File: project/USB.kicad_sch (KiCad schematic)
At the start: 13 parts, among them IC10 FT232RL, SW6 FT232 RESET, X6 SERIAL

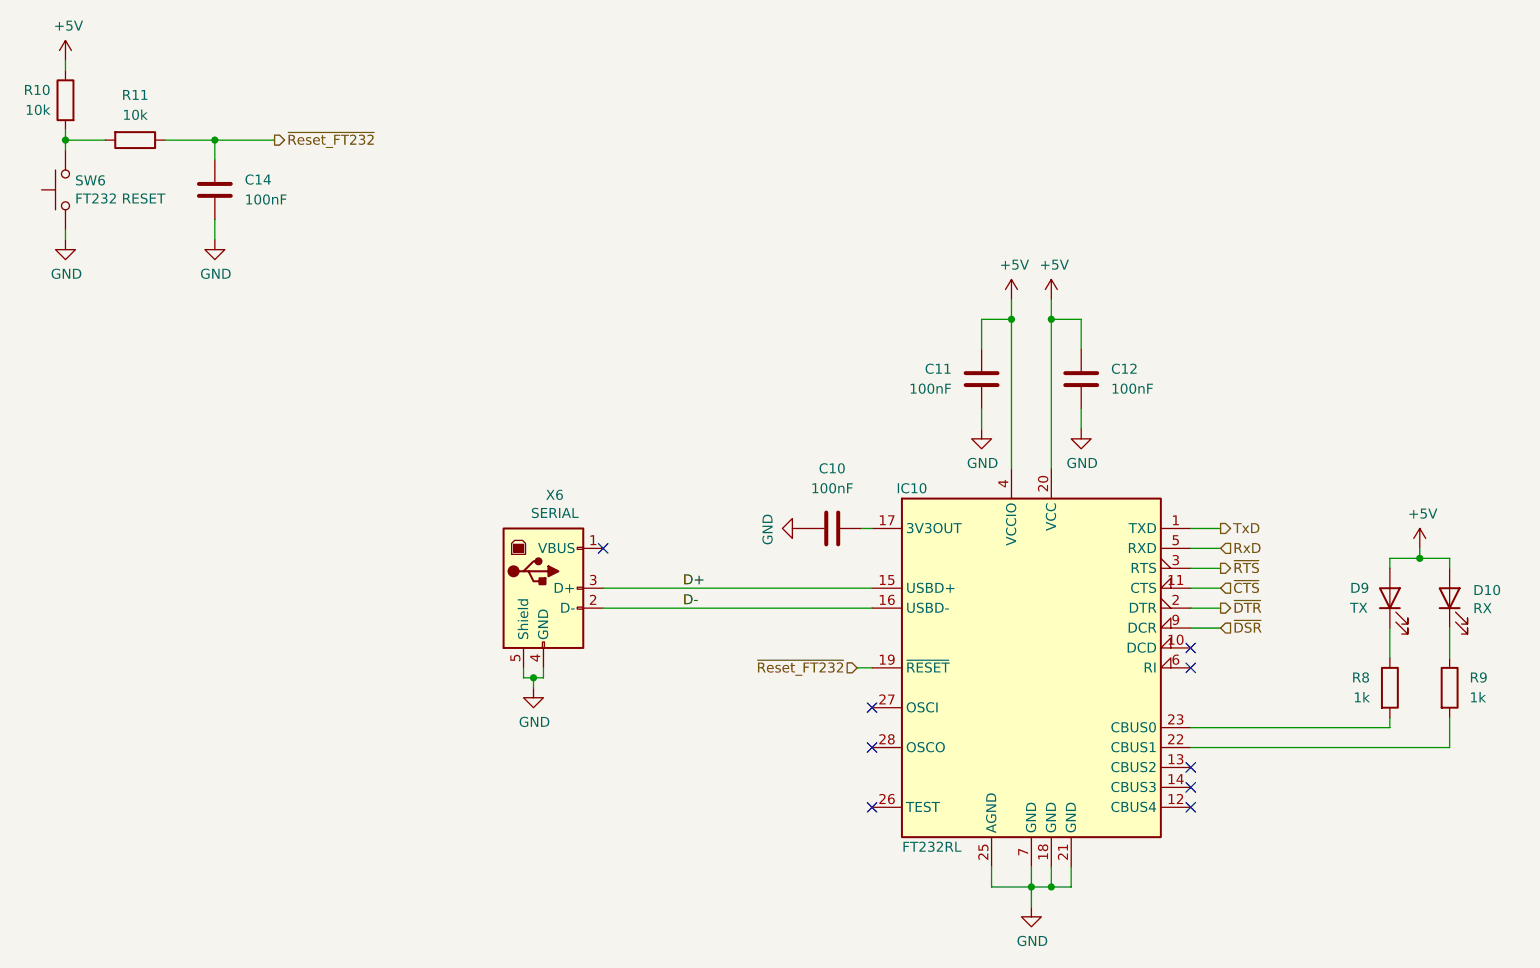
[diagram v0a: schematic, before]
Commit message: Fix grid issues, fix missing libraries, replace FT232 with FT231
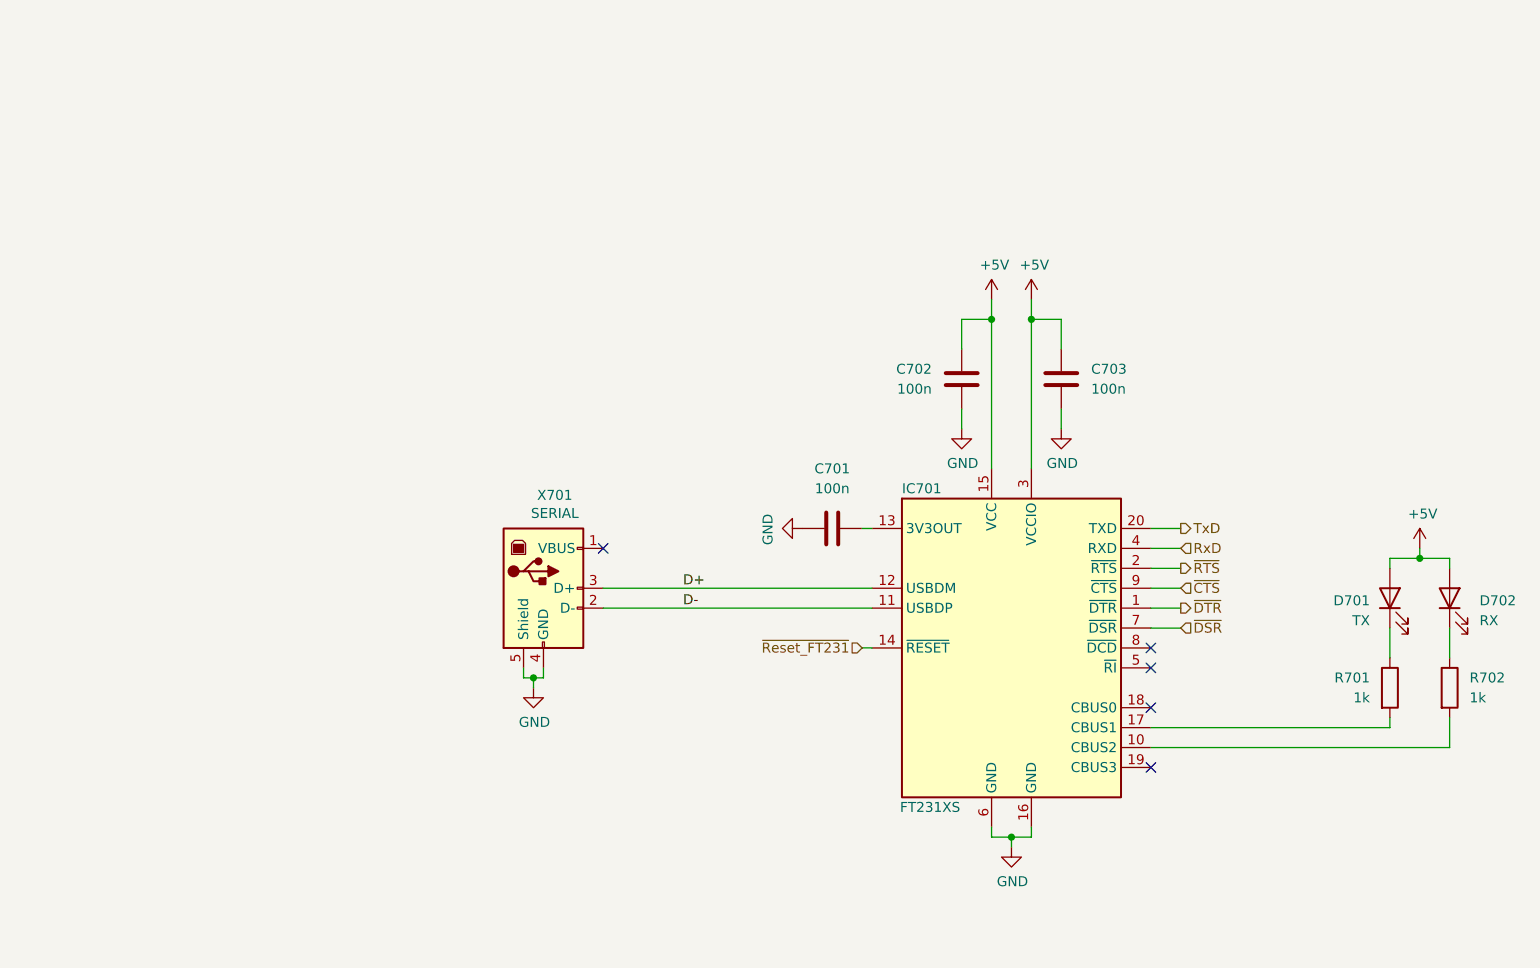
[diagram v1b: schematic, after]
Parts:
- removed C14: 100nF, Capacitor_THT:C_Rect_L4.0mm_W2.5mm_P2.50mm, symbol Device:C
- removed IC10: FT232RL, Package_SO:SSOP-28_5.3x10.2mm_P0.65mm, symbol Interface_USB:FT232RL
- removed R10, R11: 10k, Resistor_THT:R_Axial_DIN0207_L6.3mm_D2.5mm_P7.62mm_Horizontal, symbol Device:R
- removed SW6: FT232 RESET, Button_Switch_THT:SW_PUSH_6mm_H4.3mm, symbol Switch:SW_Push
- added IC701: FT231XS, Package_SO:SSOP-20_3.9x8.7mm_P0.635mm, symbol Interface_USB:FT231XS
- C701: renamed from C10; value 100nF -> 100n
- C702: renamed from C11; value 100nF -> 100n
- C703: renamed from C12; value 100nF -> 100n
- renumbered D9 to D701, D10 to D702, R8 to R701, R9 to R702, X6 to X701
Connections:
- net +5V: now also IC701.15 (VCC), IC701.3 (VCCIO)
- net D+: now also IC701.12 (USBDM)
- net D-: now also IC701.11 (USBDP)
- net GND: now also IC701.16 (GND), IC701.6 (GND)
- net RxD: now also IC701.4 (RXD)
- net TxD: now also IC701.20 (TXD)
- net ~{CTS}: now also IC701.9 (~{CTS})
- net ~{DSR}: now also IC701.7 (~{DSR})
- net ~{DTR}: now also IC701.1 (~{DTR})
- net ~{RTS}: now also IC701.2 (~{RTS})
- net at C701.2: now also IC701.13 (3V3OUT)
- net at R702.2: now also IC701.10 (CBUS2)
- net at R701.2: now also IC701.17 (CBUS1)
- new net ~{Reset_FT231}: IC701.14 (~{RESET})
- no-connect marks 9 -> 5
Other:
- moved on the sheet: C702, C703

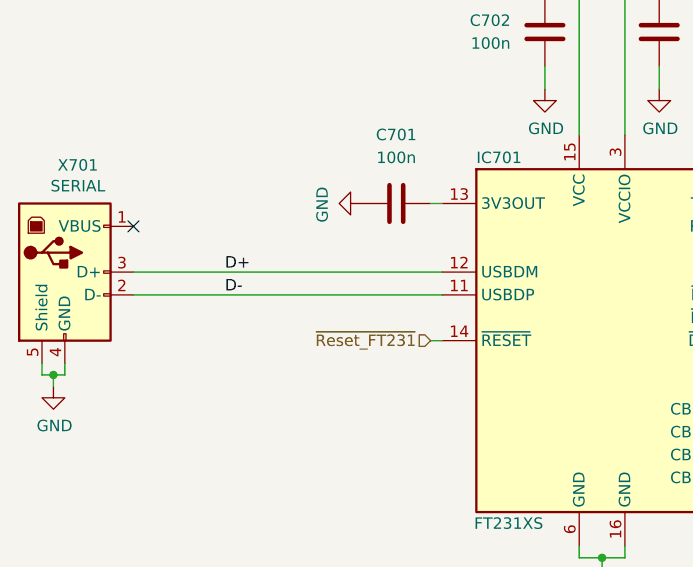
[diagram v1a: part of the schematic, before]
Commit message: Fix swapped DM and DP, add missing datasheets, remove Mouser property
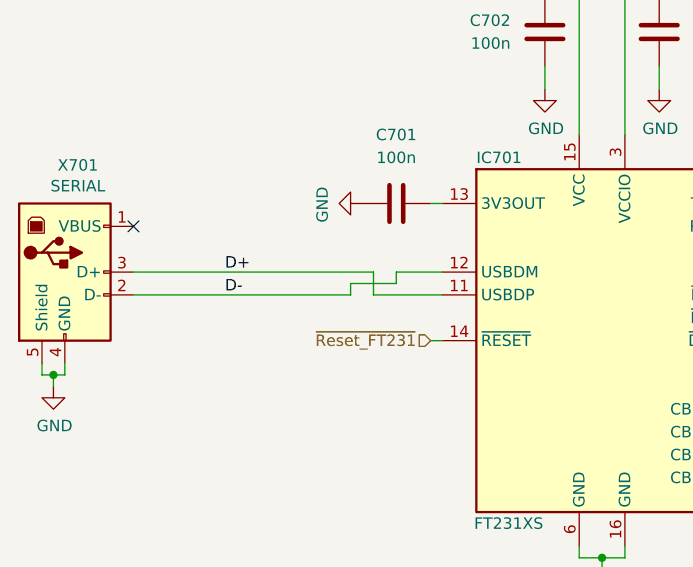
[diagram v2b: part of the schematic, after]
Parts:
- C701, C702, C703: Mouser 80-C0805C104K5R -> (none)
- D701: Mouser 604-APT2012PYW -> (none)
- D702: Mouser 604-APT2012PGW -> (none)
- R701, R702: Mfr. No. MFP-25BRD52-1K -> RT0805DRE071KL; Mouser 603-MFP-25BRD52-1K -> (none)
- X701: Mouser 571-292304-2 -> (none)
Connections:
- net D+: now also IC701.11 (USBDP); no longer IC701.12 (USBDM)
- net D-: now also IC701.12 (USBDM); no longer IC701.11 (USBDP)
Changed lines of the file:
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@@
+	(wire
+		(pts
+			(xy 113.03 88.9) (xy 118.11 88.9)
+		)
+		(stroke
+			(width 0)
+			(type default)
+		)
+	)
 	(wire
 		(pts
@@
 	(wire
 		(pts
+			(xy 88.9 87.63) (xy 115.57 87.63)
+		)
+		(stroke
+			(width 0)
+			(type default)
+		)
+	)
+	(wire
+		(pts
 			(xy 80.01 99.06) (xy 80.01 100.33)
 		)
@@
 	(wire
 		(pts
+			(xy 115.57 87.63) (xy 115.57 90.17)
+		)
+		(stroke
+			(width 0)
+			(type default)
+		)
+	)
+	(wire
+		(pts
 			(xy 121.92 95.25) (xy 123.19 95.25)
 		)
@@
 	(wire
 		(pts
+			(xy 118.11 87.63) (xy 123.19 87.63)
+		)
+		(stroke
+			(width 0)
+			(type default)
+		)
+	)
+	(wire
+		(pts
+			(xy 113.03 90.17) (xy 113.03 88.9)
+		)
+		(stroke
+			(width 0)
+			(type default)
+		)
+	)
+	(wire
+		(pts
 			(xy 134.62 57.15) (xy 134.62 53.34)
 		)
@@
 	(wire
 		(pts
-			(xy 123.19 90.17) (xy 88.9 90.17)
-		)
-		(stroke
-			(width 0)
-			(type default)
-		)
-	)
-	(wire
-		(pts
 			(xy 143.51 53.34) (xy 147.32 53.34)
 		)
@@
 	(wire
 		(pts
+			(xy 118.11 88.9) (xy 118.11 87.63)
+		)
+		(stroke
+			(width 0)
+			(type default)
+		)
+	)
+	(wire
+		(pts
 			(xy 80.01 99.06) (xy 81.28 99.06)
 		)
@@
 	(wire
 		(pts
+			(xy 88.9 90.17) (xy 113.03 90.17)
+		)
+		(stroke
+			(width 0)
+			(type default)
+		)
+	)
+	(wire
+		(pts
 			(xy 147.32 64.77) (xy 147.32 67.31)
 		)
@@
 	(wire
 		(pts
+			(xy 115.57 90.17) (xy 123.19 90.17)
+		)
+		(stroke
+			(width 0)
+			(type default)
+		)
+	)
+	(wire
+		(pts
 			(xy 189.23 92.71) (xy 189.23 96.52)
-		)
-		(stroke
-			(width 0)
-			(type default)
-		)
-	)
-	(wire
-		(pts
-			(xy 88.9 87.63) (xy 123.19 87.63)
 		)
 		(stroke
@@
 			)
 		)
-		(property "Datasheet" "~"
+		(property "Datasheet" "https://www.mouser.de/datasheet/2/418/7/ENG_CD_292304_D4-2061420.pdf"
 			(at 85.09 88.9 0)
 			(effects
@@
 		(property "Mfr. No." "292304-2"
 			(at 82.7278 75.7936 0)
-			(effects
-				(font
-					(size 1.27 1.27)
-				)
-				(hide yes)
-			)
-		)
-		(property "Mouser" "571-292304-2"
-			(at 82.7278 78.105 0)
 			(effects
 				(font
@@
 			)
 		)
-		(property "Datasheet" "~"
+		(property "Datasheet" "https://www.mouser.de/datasheet/2/447/KEM_C1002_X7R_SMD-3316098.pdf"
 			(at 134.62 60.96 0)
 			(effects
@@
 		)
 		(property "Mfr. No." "C0805C104K5RACTU"
-			(at 134.62 60.96 0)
-			(effects
-				(font
-					(size 1.27 1.27)
-				)
-				(hide yes)
-			)
-		)
-		(property "Mouser" "80-C0805C104K5R"
 			(at 134.62 60.96 0)
 			(effects
@@
 			)
 		)
-		(property "Datasheet" "~"
+		(property "Datasheet" "https://www.mouser.de/datasheet/2/447/KEM_C1002_X7R_SMD-3316098.pdf"
 			(at 147.32 60.96 0)
 			(effects
@@
 		)
 		(property "Mfr. No." "C0805C104K5RACTU"
-			(at 147.32 60.96 0)
-			(effects
-				(font
-					(size 1.27 1.27)
-				)
-				(hide yes)
-			)
-		)
-		(property "Mouser" "80-C0805C104K5R"
 			(at 147.32 60.96 0)
 			(effects
@@
 			)
 		)
-		(property "Datasheet" "~"
+		(property "Datasheet" "https://www.mouser.de/datasheet/2/216/apt2012pyw-1173287.pdf"
 			(at 189.23 88.9 0)
 			(effects
@@
 		)
 		(property "Mfr. No." "APT2012PYW"
-			(at 189.23 88.9 0)
-			(effects
-				(font
-					(size 1.27 1.27)
-				)
-				(hide yes)
-			)
-		)
-		(property "Mouser" "604-APT2012PYW"
 			(at 189.23 88.9 0)
 			(effects
@@
 			)
 		)
-		(property "Datasheet" "~"
+		(property "Datasheet" "https://www.mouser.de/datasheet/2/447/Yageo_LR_MFP_1-1947926.pdf"
 			(at 189.23 100.33 0)
 			(effects
@@
 			)
 		)
-		(property "Mfr. No." "MFP-25BRD52-1K"
-			(at 189.23 100.33 0)
-			(effects
-				(font
-					(size 1.27 1.27)
-				)
-				(hide yes)
-			)
-		)
-		(property "Mouser" "603-MFP-25BRD52-1K"
+		(property "Mfr. No." "RT0805DRE071KL"
 			(at 189.23 100.33 0)
 			(effects
@@
 			)
 		)
-		(property "Datasheet" "~"
+		(property "Datasheet" "https://www.mouser.de/datasheet/2/447/Yageo_LR_MFP_1-1947926.pdf"
 			(at 196.85 100.33 0)
 			(effects
@@
 			)
 		)
-		(property "Mfr. No." "MFP-25BRD52-1K"
-			(at 196.85 100.33 0)
-			(effects
-				(font
-					(size 1.27 1.27)
-				)
-				(hide yes)
-			)
-		)
-		(property "Mouser" "603-MFP-25BRD52-1K"
+		(property "Mfr. No." "RT0805DRE071KL"
 			(at 196.85 100.33 0)
 			(effects
@@
 			)
 		)
-		(property "Datasheet" "~"
+		(property "Datasheet" "https://www.mouser.de/datasheet/2/216/apt2012pyw-1173287.pdf"
 			(at 196.85 88.9 0)
 			(effects
@@
 		)
 		(property "Mfr. No." "APT2012PGW"
-			(at 196.85 88.9 0)
-			(effects
-				(font
-					(size 1.27 1.27)
-				)
-				(hide yes)
-			)
-		)
-		(property "Mouser" "604-APT2012PGW"
 			(at 196.85 88.9 0)
 			(effects
@@
 			)
 		)
-		(property "Datasheet" "~"
+		(property "Datasheet" "https://www.mouser.de/datasheet/2/447/KEM_C1002_X7R_SMD-3316098.pdf"
 			(at 118.11 80.01 0)
 			(effects
@@
 			(at 118.11 80.01 0)
 			(effects
-				(font
-					(size 1.27 1.27)
-				)
-				(hide yes)
-			)
-		)
-		(property "Mouser" "80-C0805C104K5R"
-			(at 118.11 80.01 0)
-			(effects
